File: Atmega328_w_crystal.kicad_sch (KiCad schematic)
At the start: 11 parts

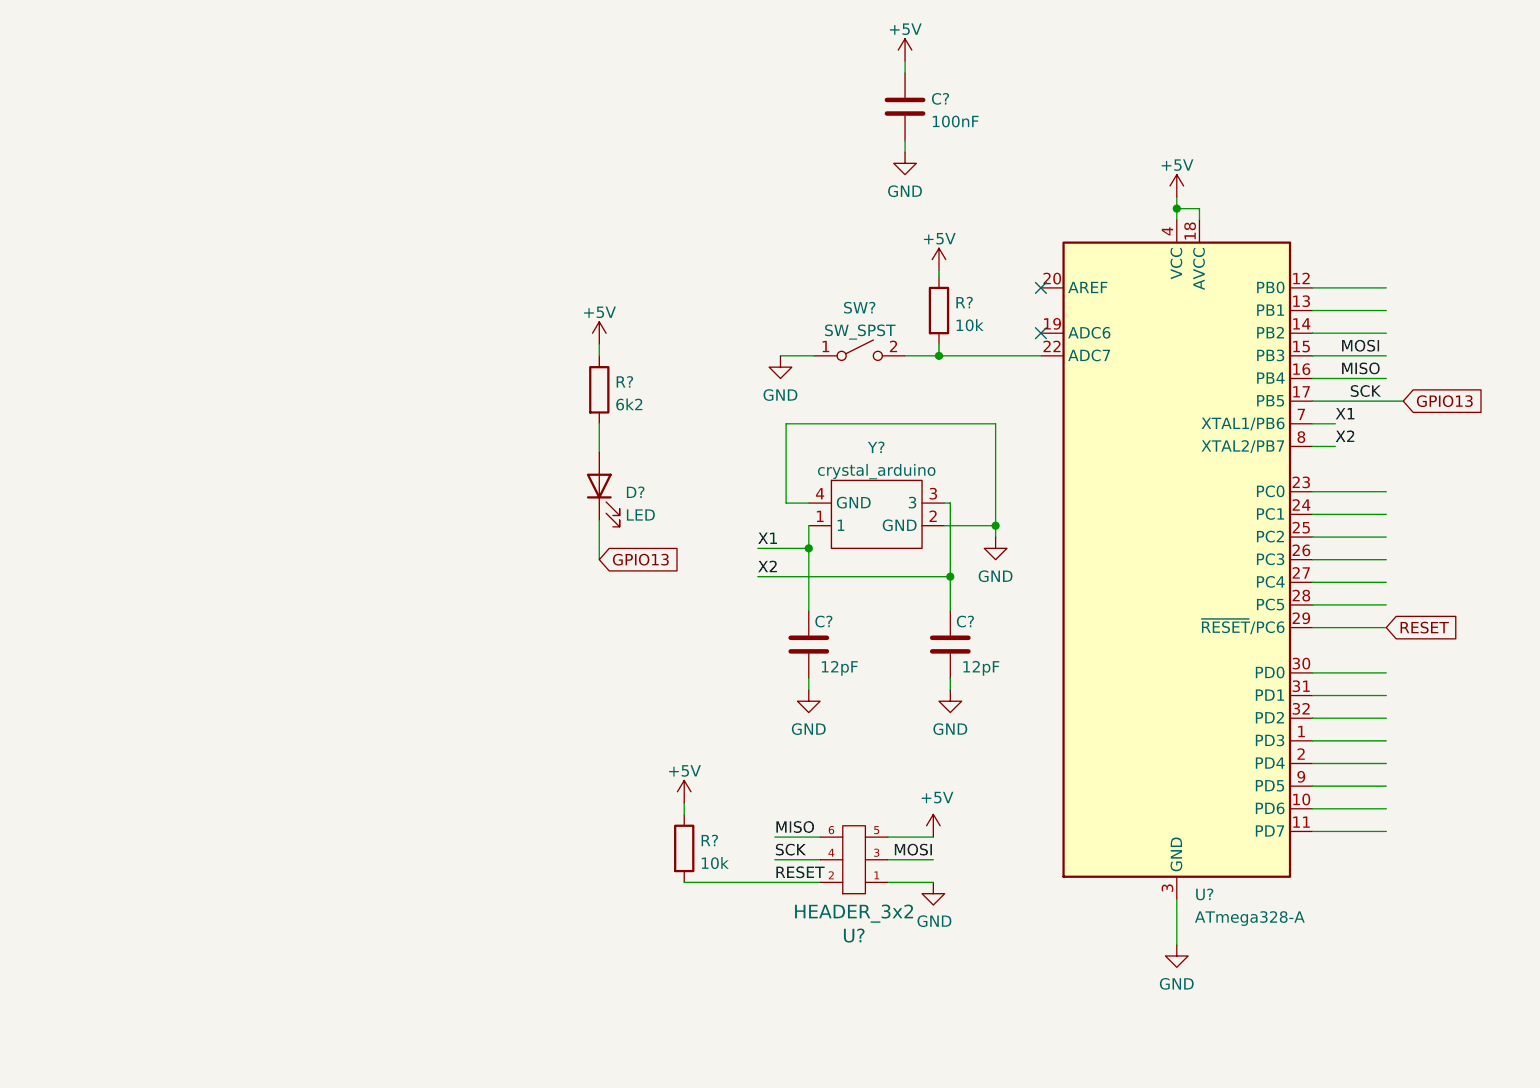
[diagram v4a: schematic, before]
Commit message: added hierarchial labels to some schematics
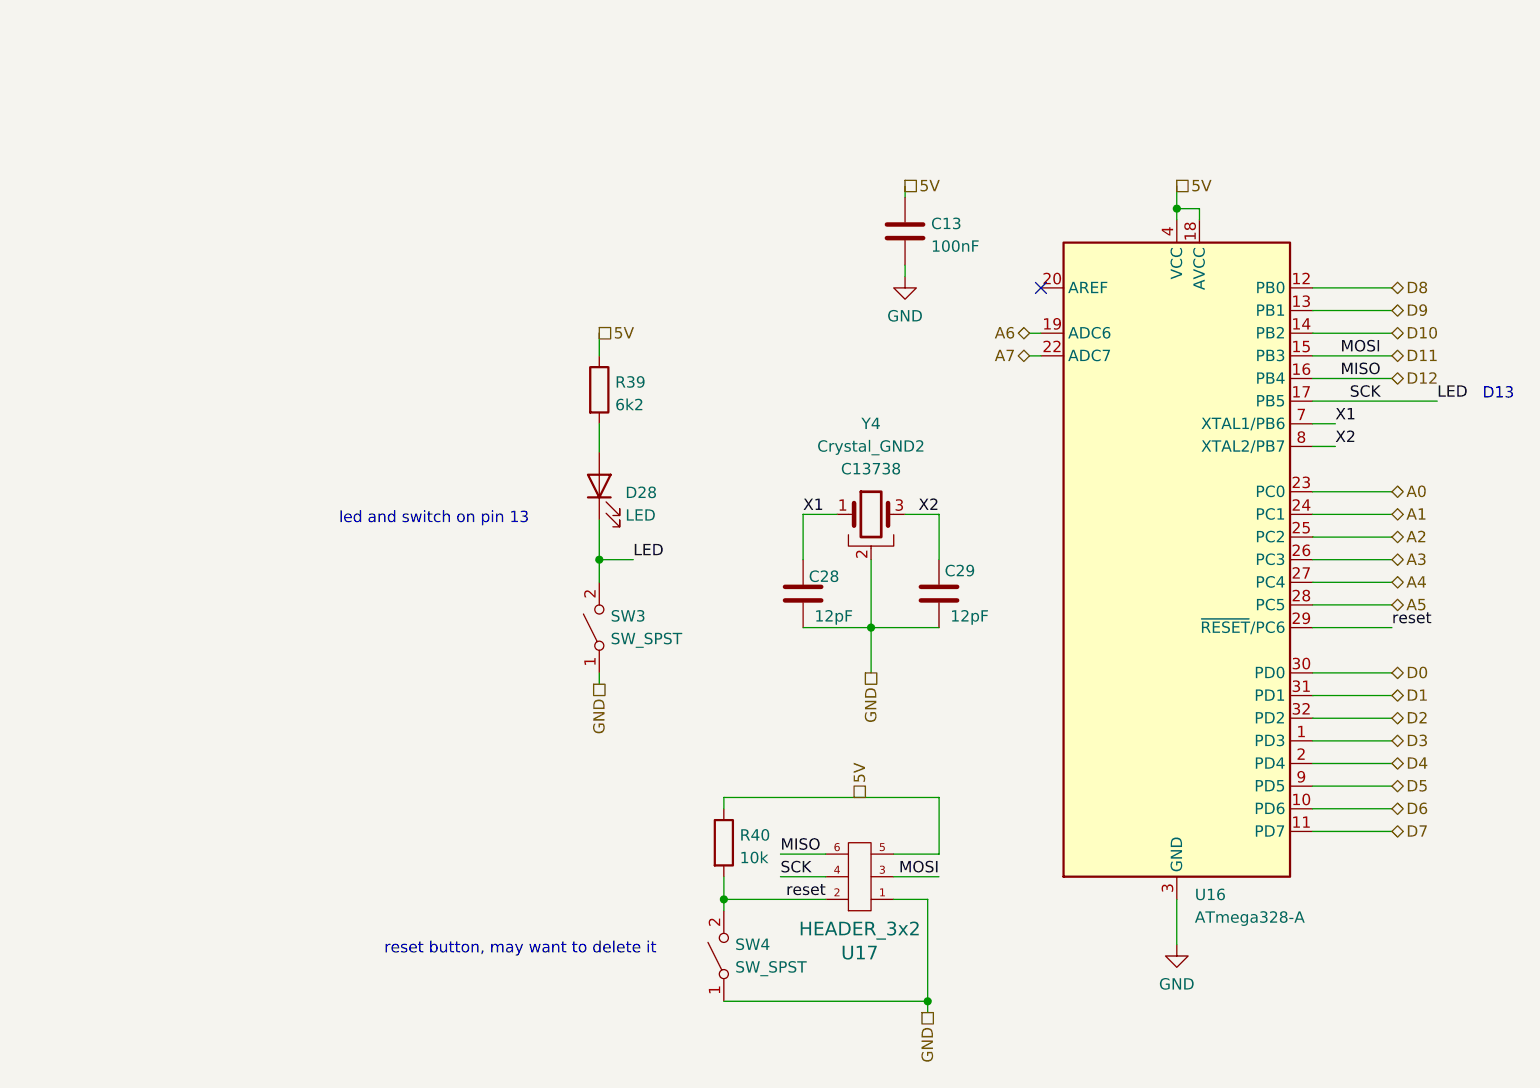
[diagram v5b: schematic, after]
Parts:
- removed C? (x2): 12pF, Capacitor_SMD:C_0402_1005Metric_Pad0.74x0.62mm_HandSolder, symbol Device:C
- removed R?: 10k, Resistor_SMD:R_0402_1005Metric_Pad0.72x0.64mm_HandSolder, symbol Device:R
- removed Y?: crystal_arduino, custom_kicad_lib_sk:crystal_arduino, symbol custom_bas:crystal_arduino
- added C28, C29: 12pF, Capacitor_SMD:C_0805_2012Metric_Pad1.18x1.45mm_HandSolder, symbol Device:C
- added SW4: SW_SPST, Button_Switch_SMD:SW_SPST_SKQG_WithStem, symbol Switch:SW_SPST
- added Y4: Crystal_GND2, custom_kicad_lib_sk:crystal_arduino, symbol custom_kicad_lib_sk:crystal_arduino
- gave numbers to parts that had none: 7
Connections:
- net GND: now also C28.1, C29.1, SW4.1 (A), Y4.2 (GND), Y4.4 (GND)
- net X1: now also C28.2, Y4.1
- net X2: now also C29.2, Y4.3
- net D3: now reaches U16.1 (PD3)
- net D6: now reaches U16.10 (PD6)
- net D7: now reaches U16.11 (PD7)
- net D8: now reaches U16.12 (PB0)
- net D9: now reaches U16.13 (PB1)
- net D10: now reaches U16.14 (PB2)
- net A6: now reaches U16.19 (ADC6)
- net D4: now reaches U16.2 (PD4)
- net A7: now reaches U16.22 (ADC7)
- net A7: no longer SW3.2 (B)
- net A0: now reaches U16.23 (PC0)
- net A1: now reaches U16.24 (PC1)
- net A2: now reaches U16.25 (PC2)
- net A3: now reaches U16.26 (PC3)
- net A4: now reaches U16.27 (PC4)
- net A5: now reaches U16.28 (PC5)
- net D0: now reaches U16.30 (PD0)
- net D1: now reaches U16.31 (PD1)
- net D2: now reaches U16.32 (PD2)
- net D5: now reaches U16.9 (PD5)
- net +5V renamed 5V
- net GPIO13 renamed LED
- net LED: now also SW3.2 (B)
- net MISO renamed D12
- net MOSI renamed D11
- net RESET renamed reset
- net reset: now also SW4.2 (B)
- no-connect marks 2 -> 1
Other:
- note added: "D13"
- note added: "led and switch on pin 13"
- note added: "reset button, may want to delete it"
- moved on the sheet: C13, R40, SW3, U17
